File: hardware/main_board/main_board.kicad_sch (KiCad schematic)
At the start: 102 parts, among them J1 USB_C_Receptacle_USB2.0_16P, J3 BAT1, J4 Conn_02x05_Odd_Even, J5 Conn_02x05_Odd_Even, Q1 MMBT3904, Q17 FDMC4435BZ, Q2 MMBT3904, SW2 XKB5858-W-E-75, SW3 XKB5858-W-E-75, U1 LTR-303ALS-01, U10 HUSB238_002DD, U11 TPS22810DBVR, U12 TPS2121, U14 BQ25601, U15 TPS63802, U17 NCH2800HV, U2 CP2102N-A02-GQFN28, U3 SRV05-4, U4 DFPlayer_mini, U5 ESP32-S3-WROOM1, U6 DS3231MZ, U7 TPS22918DBVR, U9 TPS61022

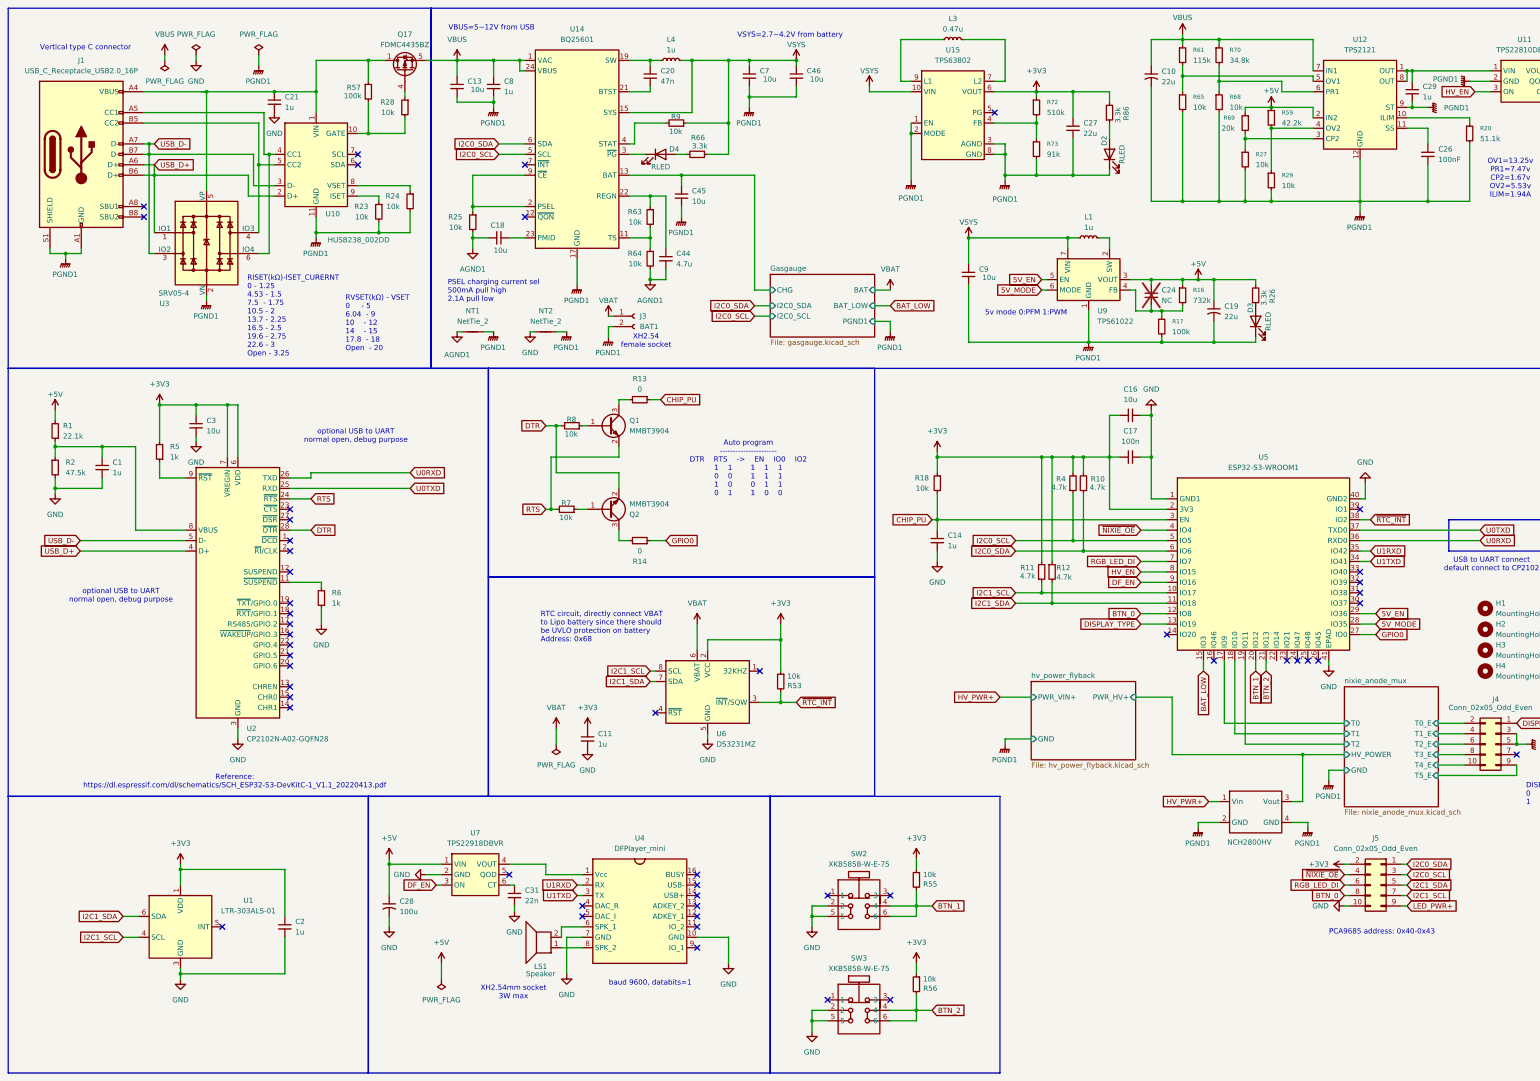
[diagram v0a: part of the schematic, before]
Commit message: hardware(sch): update schamatic and layout for next update
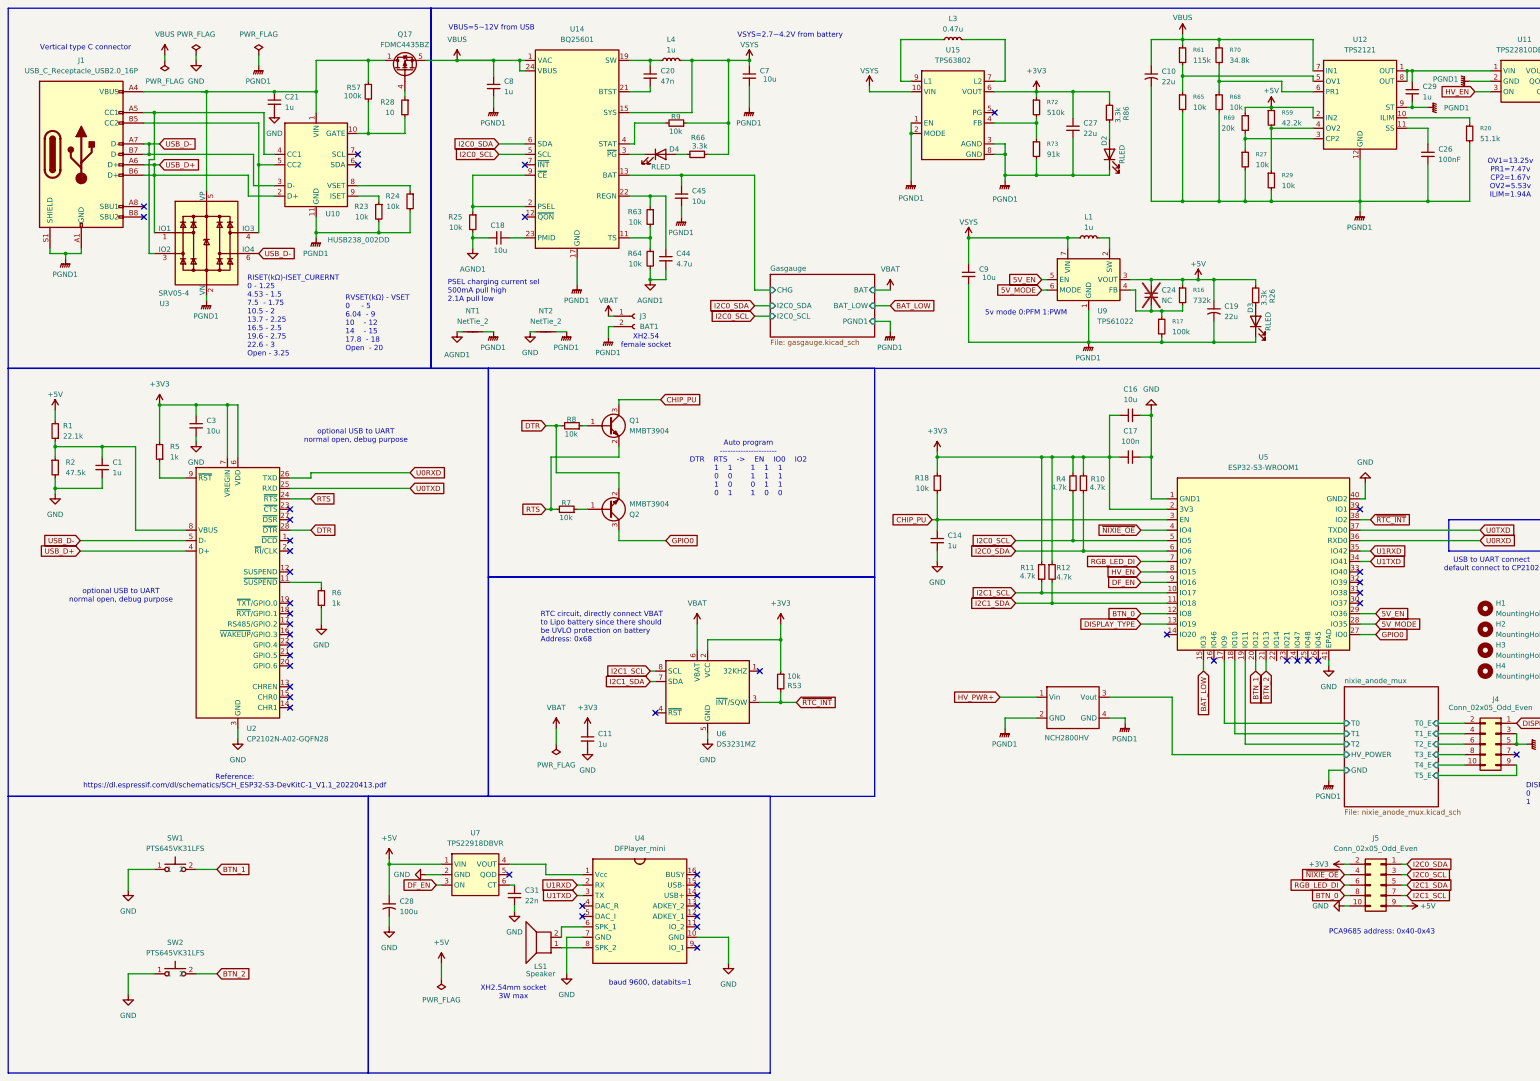
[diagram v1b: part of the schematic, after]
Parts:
- removed C13, C46: 10u, Capacitor_SMD:C_0805_2012Metric, symbol Device:C_Small
- removed C2: 1u, Capacitor_SMD:C_0603_1608Metric, symbol Device:C_Small
- removed R13, R14: 0, Resistor_SMD:R_0603_1608Metric, symbol Device:R_Small
- removed R55, R56: 10k, Resistor_SMD:R_0402_1005Metric, symbol Device:R_Small
- removed SW2, SW3: XKB5858-W-E-75, habonroof_kicad_library:XKB5858, symbol Johnson_Symbol_Lib:SW_push_RightAngle
- removed U1: LTR-303ALS-01, OptoDevice:Lite-On_LTR-303ALS-01, symbol Sensor_Optical:LTR-303ALS-01
- added SW1, SW2: PTS645VK31LFS, habonroof_kicad_library:PTS645VK31LFS, symbol Johnson_Symbol_Lib:PTS645VK31LFS
- R28: value 10k -> 10; LCSC PN C25744 -> (none)
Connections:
- net LED_PWR+ is gone; now on net +5V: J5.9 (Pin_9)
- net BTN_1: now also SW1.2
- net BTN_2: now also SW2.2
- net CHIP_PU: now also Q1.3 (C)
- net GND: now also SW1.1, SW2.1
- net GPIO0: now also Q2.3 (C)
- net USB_D-: now also U3.6 (IO4); no longer U3.3 (IO2)
- net at J1.A5 (CC1), U10.4 (CC1): now also U3.3 (IO2); no longer U3.6 (IO4)
- net hv_power_flyback/PWR_HV+ renamed nixie_anode_mux/HV_POWER
- no-connect marks 52 -> 47
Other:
- removed sheet hv_power_flyback

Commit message: WIP: update pcb and schematic
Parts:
- removed C24: NC, Capacitor_SMD:C_0603_1608Metric, symbol Device:C_Small
- added TP1, TP2: TestPoint, TestPoint:TestPoint_Pad_1.5x1.5mm, symbol Connector:TestPoint
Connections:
- net at U5.31 (IO38): now also TP2.1
- net at U5.32 (IO39): now also TP1.1
- no-connect marks 47 -> 46
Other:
- note added: "DISPLAY TYPE 0 IN-4 1 IN-14"
- note removed: "DISPLAY TYPE 0 IN-4 1 IN-18"
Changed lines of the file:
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@@
 		)
 	)
-	(text "DISPLAY TYPE\n0		IN-4\n1		IN-18"
+	(text "DISPLAY TYPE\n0		IN-4\n1		IN-14"
 		(exclude_from_sim no)
 		(at 384.556 205.232 0)
@@
 	)
 	(junction
-		(at 293.37 87.63)
-		(diameter 0)
-		(color 0 0 0 0)
-	)
-	(junction
 		(at 60.96 110.49)
 		(diameter 0)
@@
 	)
 	(junction
+		(at 300.99 80.01)
+		(diameter 0)
+		(color 0 0 0 0)
+	)
+	(junction
 		(at 190.5 26.67)
 		(diameter 0)
@@
 	)
 	(junction
-		(at 300.99 80.01)
-		(diameter 0)
-		(color 0 0 0 0)
-	)
-	(junction
 		(at 171.45 69.85)
 		(diameter 0)
@@
 	)
 	(junction
-		(at 293.37 80.01)
-		(diameter 0)
-		(color 0 0 0 0)
-	)
-	(junction
 		(at 276.86 146.05)
 		(diameter 0)
@@
 	)
 	(no_connect
-		(at 344.17 156.21)
-	)
-	(no_connect
 		(at 83.82 151.13)
 	)
@@
 	)
 	(no_connect
+		(at 323.85 172.72)
+	)
+	(no_connect
 		(at 182.88 234.95)
 	)
@@
 	)
 	(no_connect
-		(at 344.17 153.67)
-	)
-	(no_connect
 		(at 172.72 185.42)
 	)
@@
 	(wire
 		(pts
-			(xy 293.37 86.36) (xy 293.37 87.63)
-		)
-		(stroke
-			(width 0)
-			(type default)
-		)
-	)
-	(wire
-		(pts
 			(xy 181.61 26.67) (xy 181.61 39.37)
 		)
@@
 	(wire
 		(pts
-			(xy 293.37 80.01) (xy 293.37 81.28)
+			(xy 276.86 123.19) (xy 276.86 127)
 		)
 		(stroke
@@
 	(wire
 		(pts
-			(xy 276.86 123.19) (xy 276.86 127)
+			(xy 289.56 82.55) (xy 289.56 87.63)
 		)
 		(stroke
@@
 	(wire
 		(pts
-			(xy 289.56 82.55) (xy 289.56 87.63)
+			(xy 140.97 69.85) (xy 137.16 69.85)
 		)
 		(stroke
@@
 	(wire
 		(pts
-			(xy 140.97 69.85) (xy 137.16 69.85)
+			(xy 355.6 222.25) (xy 354.33 222.25)
 		)
 		(stroke
@@
 	(wire
 		(pts
-			(xy 355.6 222.25) (xy 354.33 222.25)
+			(xy 283.21 113.03) (xy 283.21 123.19)
 		)
 		(stroke
@@
 	(wire
 		(pts
-			(xy 283.21 113.03) (xy 283.21 123.19)
+			(xy 74.93 49.53) (xy 74.93 57.15)
 		)
 		(stroke
@@
 	(wire
 		(pts
-			(xy 74.93 49.53) (xy 74.93 57.15)
+			(xy 344.17 153.67) (xy 349.25 153.67)
 		)
 		(stroke
@@
 	(wire
 		(pts
-			(xy 288.29 80.01) (xy 293.37 80.01)
-		)
-		(stroke
-			(width 0)
-			(type default)
-		)
-	)
-	(wire
-		(pts
 			(xy 203.2 180.34) (xy 203.2 182.88)
 		)
@@
 	(wire
 		(pts
-			(xy 289.56 87.63) (xy 293.37 87.63)
+			(xy 289.56 87.63) (xy 295.91 87.63)
 		)
 		(stroke
@@
 	(wire
 		(pts
-			(xy 293.37 87.63) (xy 295.91 87.63)
-		)
-		(stroke
-			(width 0)
-			(type default)
-		)
-	)
-	(wire
-		(pts
 			(xy 360.68 60.96) (xy 344.17 60.96)
 		)
@@
 	(wire
 		(pts
-			(xy 293.37 80.01) (xy 300.99 80.01)
-		)
-		(stroke
-			(width 0)
-			(type default)
-		)
-	)
-	(wire
-		(pts
 			(xy 196.85 82.55) (xy 196.85 54.61)
 		)
@@
 	(wire
 		(pts
+			(xy 344.17 156.21) (xy 349.25 156.21)
+		)
+		(stroke
+			(width 0)
+			(type default)
+		)
+	)
+	(wire
+		(pts
 			(xy 241.3 127) (xy 241.3 123.19)
 		)
@@
 	(wire
 		(pts
+			(xy 288.29 80.01) (xy 300.99 80.01)
+		)
+		(stroke
+			(width 0)
+			(type default)
+		)
+	)
+	(wire
+		(pts
 			(xy 50.8 54.61) (xy 73.66 54.61)
 		)
@@
 	)
 	(symbol
+		(lib_id "Connector:TestPoint")
+		(at 349.25 153.67 270)
+		(unit 1)
+		(exclude_from_sim no)
+		(in_bom yes)
+		(on_board yes)
+		(dnp no)
+		(fields_autoplaced yes)
+		(property "Reference" "TP1"
+			(at 354.33 152.3999 90)
+			(effects
+				(font
+					(size 1.27 1.27)
+				)
+				(justify left)
+			)
+		)
+		(property "Value" "TestPoint"
+			(at 354.33 154.9399 90)
+			(effects
+				(font
+					(size 1.27 1.27)
+				)
+				(justify left)
+				(hide yes)
+			)
+		)
+		(property "Footprint" "TestPoint:TestPoint_Pad_1.5x1.5mm"
+			(at 349.25 158.75 0)
+			(effects
+				(font
+					(size 1.27 1.27)
+				)
+				(hide yes)
+			)
+		)
+		(property "Datasheet" "~"
+			(at 349.25 158.75 0)
+			(effects
+				(font
+					(size 1.27 1.27)
+				)
+				(hide yes)
+			)
+		)
+		(property "Description" "test point"
+			(at 349.25 153.67 0)
+			(effects
+				(font
+					(size 1.27 1.27)
+				)
+				(hide yes)
+			)
+		)
+		(pin "1"
+		)
+		(instances
+			(project ""
+				(path "/62950e93-3f98-4dee-9256-8213caa98ee7"
+					(reference "TP1")
+					(unit 1)
+				)
+			)
+		)
+	)
+	(symbol
 		(lib_id "power:GND")
 		(at 138.43 233.68 0)
@@
 	(symbol
 		(lib_id "Device:C_Small")
-		(at 293.37 83.82 0)
-		(unit 1)
-		(exclude_from_sim no)
-		(in_bom no)
-		(on_board yes)
-		(dnp yes)
-		(fields_autoplaced yes)
-		(property "Reference" "C24"
-			(at 295.91 82.5562 0)
-			(effects
-				(font
-					(size 1.27 1.27)
-				)
-				(justify left)
-			)
-		)
-		(property "Value" "NC"
-			(at 295.91 85.0962 0)
-			(effects
-				(font
-					(size 1.27 1.27)
-				)
-				(justify left)
-			)
-		)
-		(property "Footprint" "Capacitor_SMD:C_0603_1608Metric"
-			(at 293.37 83.82 0)
-			(effects
-				(font
-					(size 1.27 1.27)
-				)
-				(hide yes)
-			)
-		)
-		(property "Datasheet" "~"
-			(at 293.37 83.82 0)
-			(effects
-				(font
-					(size 1.27 1.27)
-				)
-				(hide yes)
-			)
-		)
-		(property "Description" "Unpolarized capacitor, small symbol"
-			(at 293.37 83.82 0)
-			(effects
-				(font
-					(size 1.27 1.27)
-				)
-				(hide yes)
-			)
-		)
-		(pin "1"
-		)
-		(pin "2"
-		)
-		(instances
-			(project "main_board"
-				(path "/62950e93-3f98-4dee-9256-8213caa98ee7"
-					(reference "C24")
-					(unit 1)
-				)
-			)
-		)
-	)
-	(symbol
-		(lib_id "Device:C_Small")
 		(at 394.97 38.1 0)
 		(unit 1)
@@
 					(unit 1)
 				)
+			)
+		)
+	)
+	(symbol
+		(lib_id "Connector:TestPoint")
+		(at 349.25 156.21 270)
+		(unit 1)
+		(exclude_from_sim no)
+		(in_bom yes)
+		(on_board yes)
+		(dnp no)
+		(fields_autoplaced yes)
+		(property "Reference" "TP2"
+			(at 354.33 154.9399 90)
+			(effects
+				(font
+					(size 1.27 1.27)
+				)
+				(justify left)
+			)
+		)
+		(property "Value" "TestPoint"
+			(at 354.33 157.4799 90)
+			(effects
+				(font
+					(size 1.27 1.27)
+				)
+				(justify left)
+				(hide yes)
+			)
+		)
+		(property "Footprint" "TestPoint:TestPoint_Pad_1.5x1.5mm"
+			(at 349.25 161.29 0)
+			(effects
+				(font
+					(size 1.27 1.27)
+				)
+				(hide yes)
+			)
+		)
+		(property "Datasheet" "~"
+			(at 349.25 161.29 0)
+			(effects
+				(font
+					(size 1.27 1.27)
+				)
+				(hide yes)
+			)
+		)
+		(property "Description" "test point"
+			(at 349.25 156.21 0)
+			(effects
+				(font
+					(size 1.27 1.27)
+				)
+				(hide yes)
+			)
+		)
+		(pin "1"
+		)
+		(instances
+			(project "main_board"
+				(path "/62950e93-3f98-4dee-9256-8213caa98ee7"
+					(reference "TP2")
+					(unit 1)
+				)

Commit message: WIP: schematic and layout
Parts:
- added SW1: PTS645VK31LFS, habonroof_kicad_library:PTS645VK31LFS, symbol Johnson_Symbol_Lib:PTS645VK31LFS
- renumbered SW1 to SW2, SW2 to SW3
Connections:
- net BTN_0: now also SW1.2; no longer J5.8 (Pin_8)
- net GND: now also SW1.1
- net PGND1: no longer J4.5 (Pin_5)
- net nixie_anode_mux/T6_E: now reaches J4.7 (Pin_7)
- new net nixie_anode_mux/T7_E: J4.5 (Pin_5)
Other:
- sheet nixie_anode_mux ports: added T6_E, T7_E; removed none
- note added: "DISPLAY TYPE 0V IN-4 1.65V IN-14(8pcs) 3.3V IN-14"
- note removed: "DISPLAY TYPE 0 IN-4 1 IN-14"
- moved on the sheet: SW2, SW3

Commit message: WIP: hardware layout
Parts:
- C29: LCSC PN C15849 -> C5199872
- TP1, TP2: now left out of the parts list
